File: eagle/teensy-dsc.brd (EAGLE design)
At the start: 35.2 x 51.2 mm, 7 parts, among them M1 XBEERX-VN

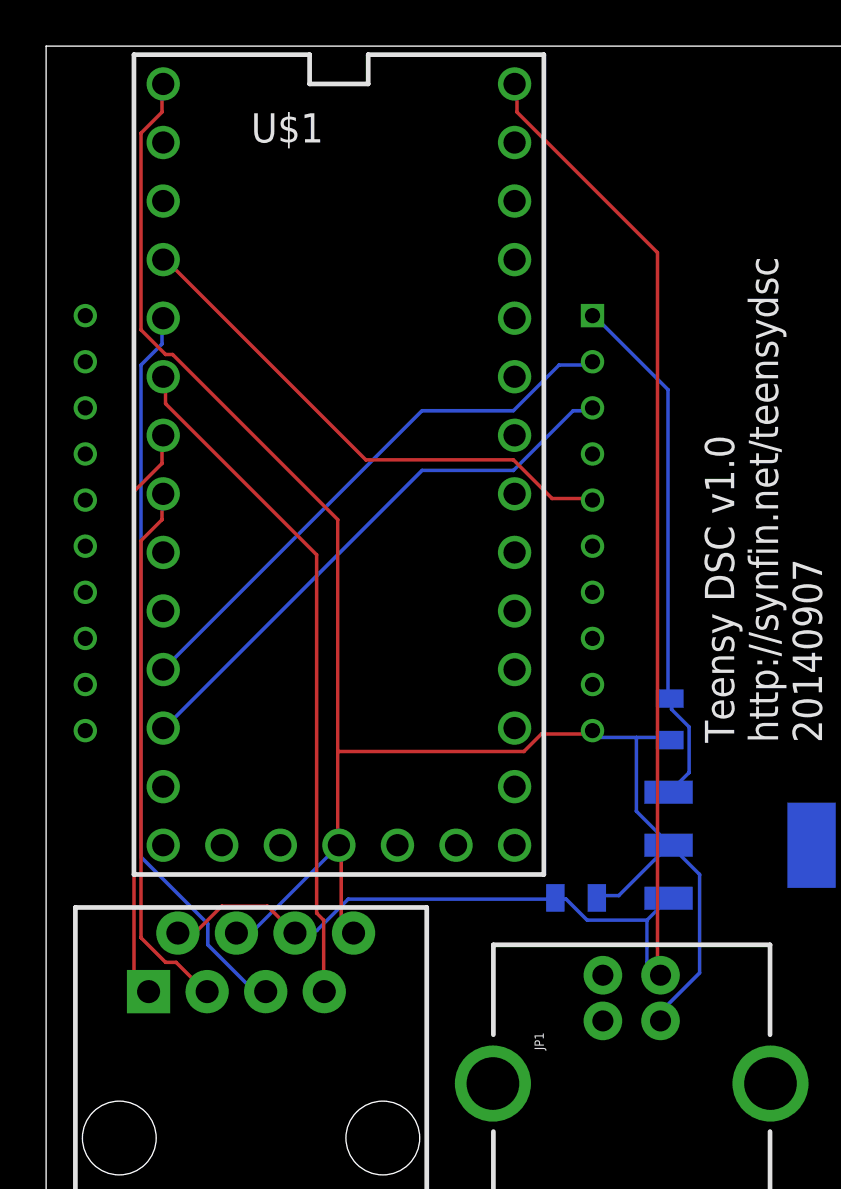
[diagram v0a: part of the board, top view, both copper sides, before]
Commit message: updated with:
- latest WiFly board
- Thicker traces for routing 5V & GND
- Removed wiring for 3.3V on Teensy 3.1 board
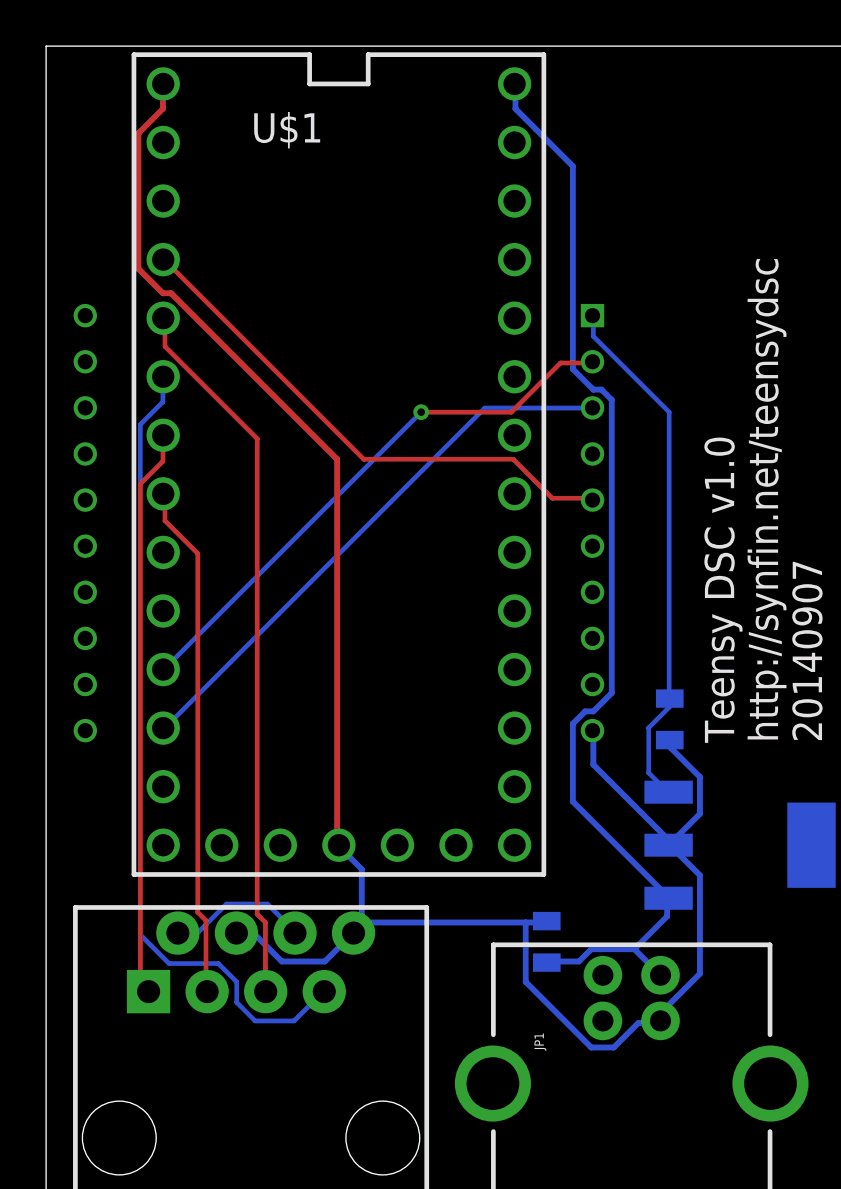
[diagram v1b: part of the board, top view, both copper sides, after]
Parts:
- moved C2 2.29 mm to (21.7, 12.3), turned to 270 degrees
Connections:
- new net S$1: JP2.2, JP2.6
- net 3.3V: no longer U$1.3.3V, U$1.3.3V1
- net 5V: no longer JP2.2, JP2.6
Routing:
- net 5V: track 67.7 -> 48.4 mm
- net GND: track 80.5 -> 87.4 mm
- net S$1: track 0.00 -> 6.25 mm
- net CHAN-A-ALT/DEC: track 29.6 -> 35.2 mm
- net CHAN-B-ALT/DEC: track 32.1 -> 31.0 mm
- net CHAN-A-AZ/RA: track 23.5 -> 22.4 mm
- net N$2: track 24.2 -> 24.1 mm, vias 0 -> 1
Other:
- board text added: "S/N:"

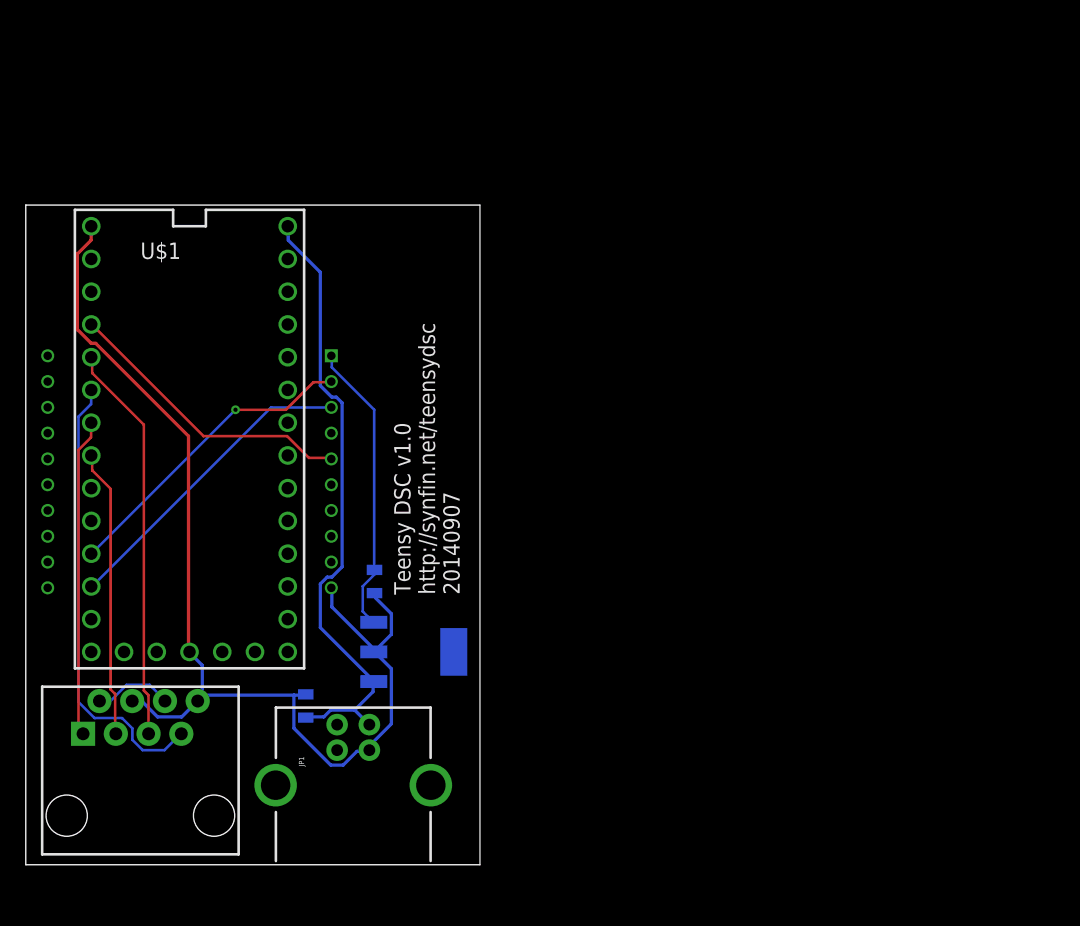
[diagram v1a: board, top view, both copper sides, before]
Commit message: New board design: - Add 2x serial ports - Add camera trigger (opto-isolated) - Add 2x external button/switch - Add dedicated program button Remove old PCB design files Start work on TeensyDSC code
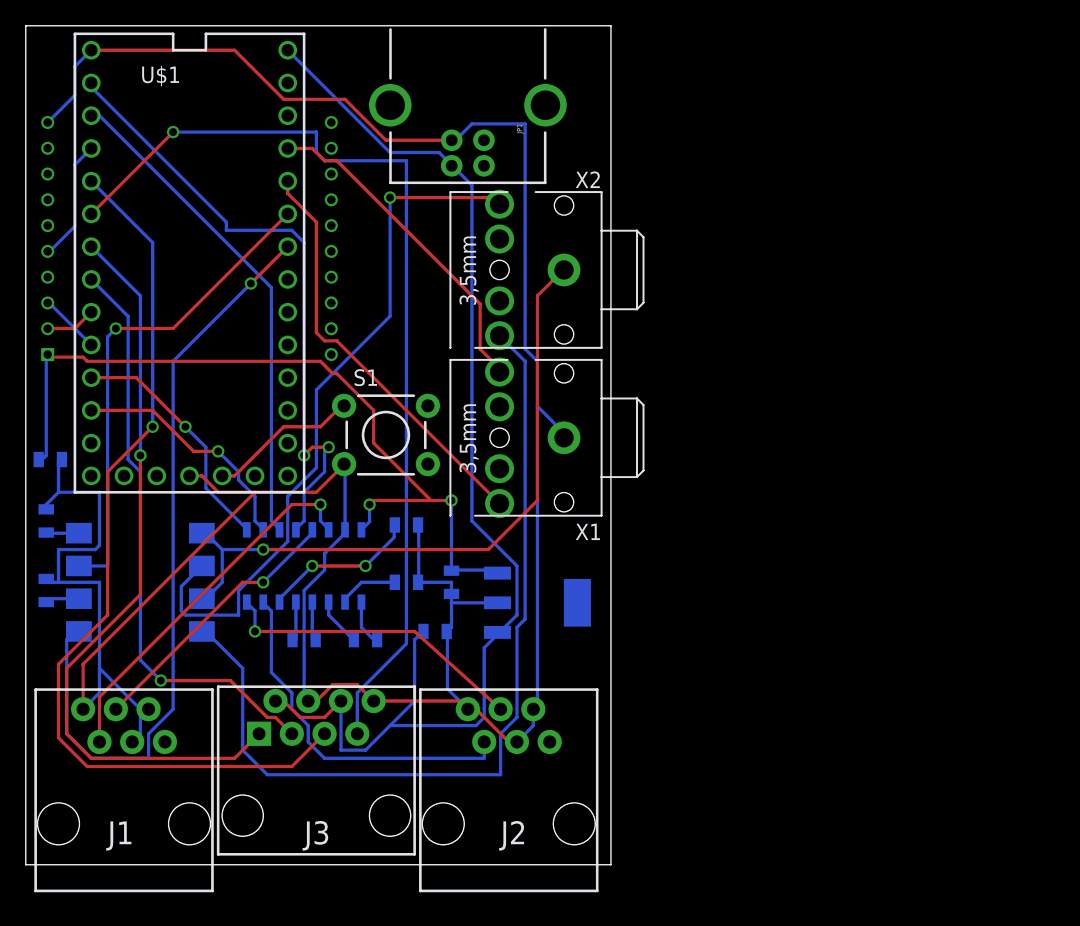
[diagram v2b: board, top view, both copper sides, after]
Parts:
- removed JP2: RJ45-8PTH, SparkFun-Connectors:RJ45-8
- added C3, C4, C5, C6, C7: 0.1uF, SparkFun-Passives:0805
- added J1, J2: RJ11-6PTH, SparkFun-Connectors:RJ11-6
- added J3: RJ45-8PTH, SparkFun-Connectors:RJ45-8
- added OK1: LTV826S, optocoupler:DIL8-SMD
- added R1, R2: 470, SparkFun-Resistors:0805
- added S1: PGM, SparkFun-Electromechanical:TACTILE-PTH
- added U$2: MAX3232IDW, SparkFun-DigitalIC:SO016
- added X1, X2: STEREOJACK, adafruit:STX3100
- moved JP1 48.1 mm to (34.3, 56.2), turned to 270 degrees
- moved C1 26.9 mm to (1.91, 31.4), turned to 180 degrees
- moved M1 21.3 mm to (15.2, 49.8), turned to 180 degrees
- moved U$1 13.7 mm to (12.7, 46.7)
- moved C2 11.6 mm to (31.8, 18.1), turned to 0 degrees
- moved U$3 10.3 mm to (39.7, 20.3)
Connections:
- net N$3 renamed XBEE_RST
- removed net S$1: JP2.2, JP2.6
- removed net VBAT: U$1.VBAT
- new net FOCUS: OK1.8, X2.2
- new net FOCUS-CTL: OK1.1, U$1.20/A6
- new net N$3: C3.1, U$2.4
- new net N$4: C3.2, U$2.5
- new net N$5: C7.1, U$2.6
- new net N$6: C6.1, U$2.2
- new net N$7: OK1.4, R2.2
- new net N$8: S1.1, U$1.PGM
- new net N$9: OK1.2, R1.2
- new net RS1-RX: J1.3, U$2.13
- new net RS1-TX: J1.2, U$2.14
- new net RS2-RX: J2.3, U$2.8
- new net RS2-TX: J2.2, U$2.7
- new net SERIAL1-RX: U$1.0, U$2.12
- new net SERIAL1-TX: U$1.1, U$2.11
- new net SERIAL2-RX: U$1.9, U$2.9
- new net SERIAL2-TX: U$1.10, U$2.10
- new net SHUTTER: OK1.6, X2.5
- new net SHUTTER-CTL: OK1.3, U$1.21/A7
- new net SHUTTER-GND: OK1.5, OK1.7, X2.1
- new net SW1: U$1.22/A8, X1.2
- new net SW2: U$1.23/A9, X1.5
- new net XBEE_IN: M1.3, U$1.8
- new net XBEE_OUT: M1.2, U$1.7
- net 3.3V: now also C5.1, U$2.16
- net 5V: now also J3.2, J3.6
- net CHAN-A-ALT/DEC: now also J3.7; no longer JP2.7
- net CHAN-A-AZ/RA: now also J3.3; no longer JP2.3
- net CHAN-B-ALT/DEC: now also J3.5; no longer JP2.5
- net CHAN-B-AZ/RA: now also J3.1; no longer JP2.1
- net GND: now also C5.2, C6.2, C7.2, J1.1, J1.4, J1.5, J2.1, J2.4, J2.5, J3.4, J3.8, R1.1, R2.1, S1.3, U$2.15, X1.1; no longer JP2.4, JP2.8
- net N$1: now also C4.1, U$2.1; no longer M1.3, U$1.10
- net N$2: now also C4.2, U$2.3; no longer M1.2, U$1.9
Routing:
- net GND: track 87.4 -> 233.1 mm
- net FOCUS: track 0.00 -> 67.2 mm
- net FOCUS-CTL: track 0.00 -> 59.8 mm, vias 0 -> 1
- net SHUTTER: track 0.00 -> 54.7 mm, vias 0 -> 1
- net SHUTTER-GND: track 0.00 -> 51.5 mm, vias 0 -> 1
- net SERIAL1-RX: track 0.00 -> 48.3 mm, vias 0 -> 2
- net 5V: track 48.4 -> 93.0 mm
- net 3.3V: track 22.8 -> 62.6 mm, vias 0 -> 2
- net CHAN-A-ALT/DEC: track 35.2 -> 75.0 mm, vias 0 -> 1
- net CHAN-B-ALT/DEC: track 31.0 -> 70.8 mm, vias 0 -> 1
- net SERIAL1-TX: track 0.00 -> 38.5 mm
- net SHUTTER-CTL: track 0.00 -> 37.9 mm, vias 0 -> 1
- net CHAN-B-AZ/RA: track 24.7 -> 58.2 mm, vias 0 -> 1
- net SW1: track 0.00 -> 32.7 mm
- net RS1-TX: track 0.00 -> 29.0 mm, vias 0 -> 1
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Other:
- board size 35.2 x 51.2 mm -> 45.4 x 65.1 mm
- board text added: "J1"
- board text added: "J2"
- board text added: "J3"
- board text added: "Teensy DSC v1.0 http://synfin.net/teensydsc 20140908"
- board text removed: "Teensy DSC v1.0 http://synfin.net/teensydsc 20140907"

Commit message: Mark board v0.2 Add a warning so people don't think it's ready for prime-time.
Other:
- board text added: "Teensy DSC v0.2 http://synfin.net/teensydsc 20140908"
- board text removed: "Teensy DSC v1.0 http://synfin.net/teensydsc 20140908"
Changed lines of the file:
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@@
 <text x="36.83" y="1.5875" size="1.778" layer="25">J2</text>
 <text x="21.59" y="1.5875" size="1.778" layer="25">J3</text>
-<text x="18.415" y="8.255" size="1.016" layer="26" rot="MR180">Teensy DSC v1.0
+<text x="18.415" y="8.255" size="1.016" layer="26" rot="MR180">Teensy DSC v0.2
 http://synfin.net/teensydsc
 20140908</text>

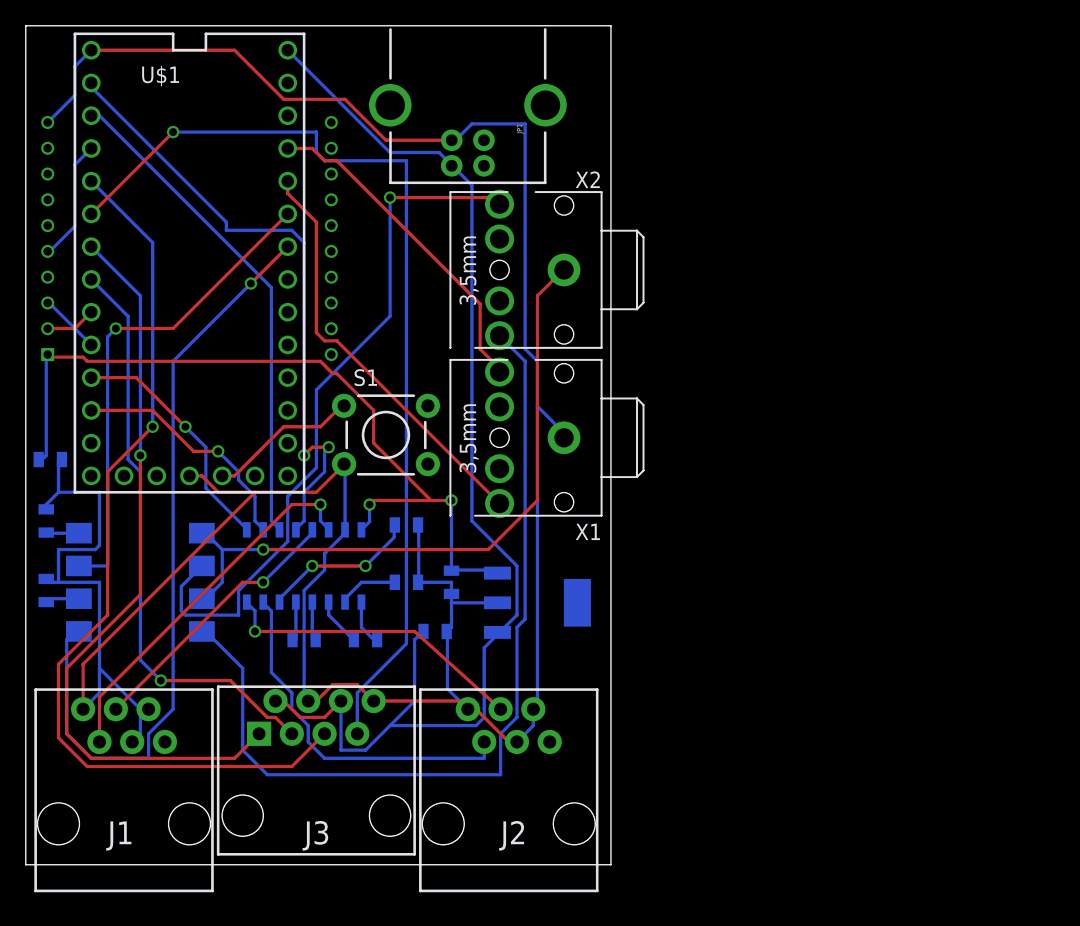
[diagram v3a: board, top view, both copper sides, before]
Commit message: Update board design with: - Remove program button since USB host mode isn't supported - Add 5mm barrel connector for ~12V power - Add necessary reverse polarity protection & regulation for 12V power - Add a frame to the .sch file
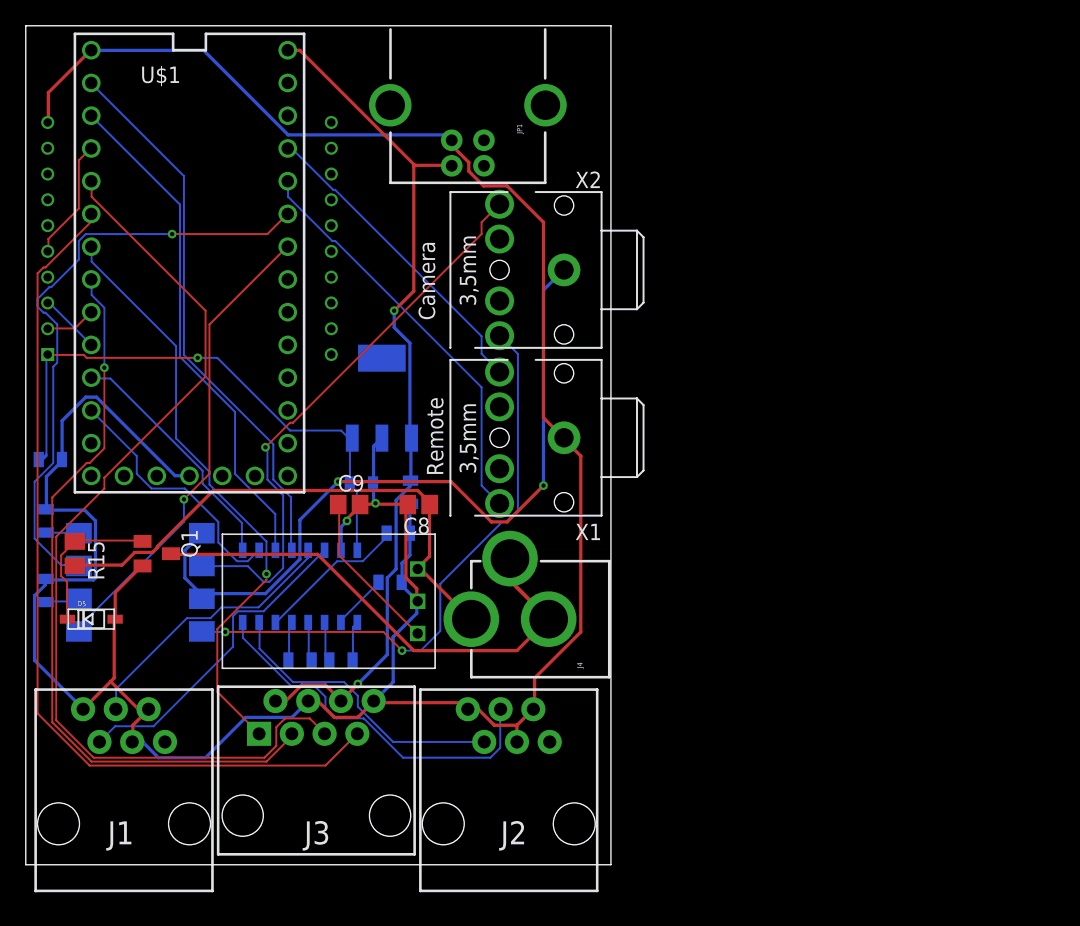
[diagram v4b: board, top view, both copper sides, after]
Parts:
- removed S1: PGM, SparkFun-Electromechanical:TACTILE-PTH
- added C8, C9: 10uF, resistor:C0805
- added D5: 10V Z, adafruit:SOD-123
- added J4: POWER_JACKPTH, SparkFun-Connectors:POWER_JACK_PTH
- added Q1: IRLML6344, synfinatic:SOT23
- added R15: 13.3k, resistor:M0805
- added U$4: OKI-78SR, synfinatic:OKI-78SR-H
- moved U$3 19.9 mm to (27.6, 36.2), turned to 0 degrees
- moved C2 11.0 mm to (29.8, 28.9), turned to 90 degrees
- moved C5 10.3 mm to (26.0, 29.5), turned to 180 degrees
- moved C4 2.48 mm to (24.4, 15.9)
- moved C3 1.62 mm to (21.3, 15.9)
- moved U$2 1.62 mm to (21.3, 21.6)
- moved C6 1.27 mm to (28.3, 21.9)
- moved C7 0.90 mm to (28.9, 25.7)
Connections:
- removed net N$8: S1.1, U$1.PGM
- new net +12V: C8.1, J4.PWR, R15.2, U$4.P$1
- new net 12V: C2.2, J3.2, J3.6, JP1.VBUS, U$1.VIN, U$3.1
- new net GND_MAIN: J4.GND, J4.GNDBREAK, Q1.3
- new net N$17: D5.C, Q1.1, R15.1
- net 5V: now also C9.1, U$4.P$3; no longer C2.2, J3.2, J3.6, JP1.VBUS, U$1.VIN, U$3.1
- net GND: now also C8.2, C9.2, D5.A, Q1.2, U$4.P$2; no longer S1.3
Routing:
- net 5V: track 93.0 -> 12.6 mm
- net 12V: track 0.00 -> 67.6 mm, vias 0 -> 2
- net +12V: track 0.00 -> 41.8 mm
- net GND_MAIN: track 0.00 -> 39.4 mm
- net FOCUS-CTL: track 59.8 -> 36.6 mm
- net FOCUS: track 67.2 -> 45.9 mm, vias 0 -> 2
- net 3.3V: track 62.6 -> 44.0 mm, vias 2 -> 1
- net CHAN-A-AZ/RA: track 45.2 -> 57.4 mm
- net N$17: track 0.00 -> 12.0 mm
- net CHAN-B-AZ/RA: track 58.2 -> 46.3 mm
- net N$8: track 11.7 -> 0.00 mm
- net SHUTTER: track 54.7 -> 43.7 mm
- net SHUTTER-CTL: track 37.9 -> 47.4 mm
- net CHAN-A-ALT/DEC: track 75.0 -> 68.1 mm, vias 1 -> 0
- net SHUTTER-GND: track 51.5 -> 58.3 mm, vias 1 -> 2
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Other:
- board text added: "Camera"
- board text added: "Remote"
